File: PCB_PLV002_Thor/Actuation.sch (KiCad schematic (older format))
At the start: 58 parts, among them J20 Conn_01x02, J21 Conn_01x02, J22 Conn_01x02, J23 Conn_01x02, J24 Conn_01x02, J25 Conn_01x02, J26 Conn_01x02, J27 Conn_01x02, J28 Conn_01x02, J29 Conn_01x02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

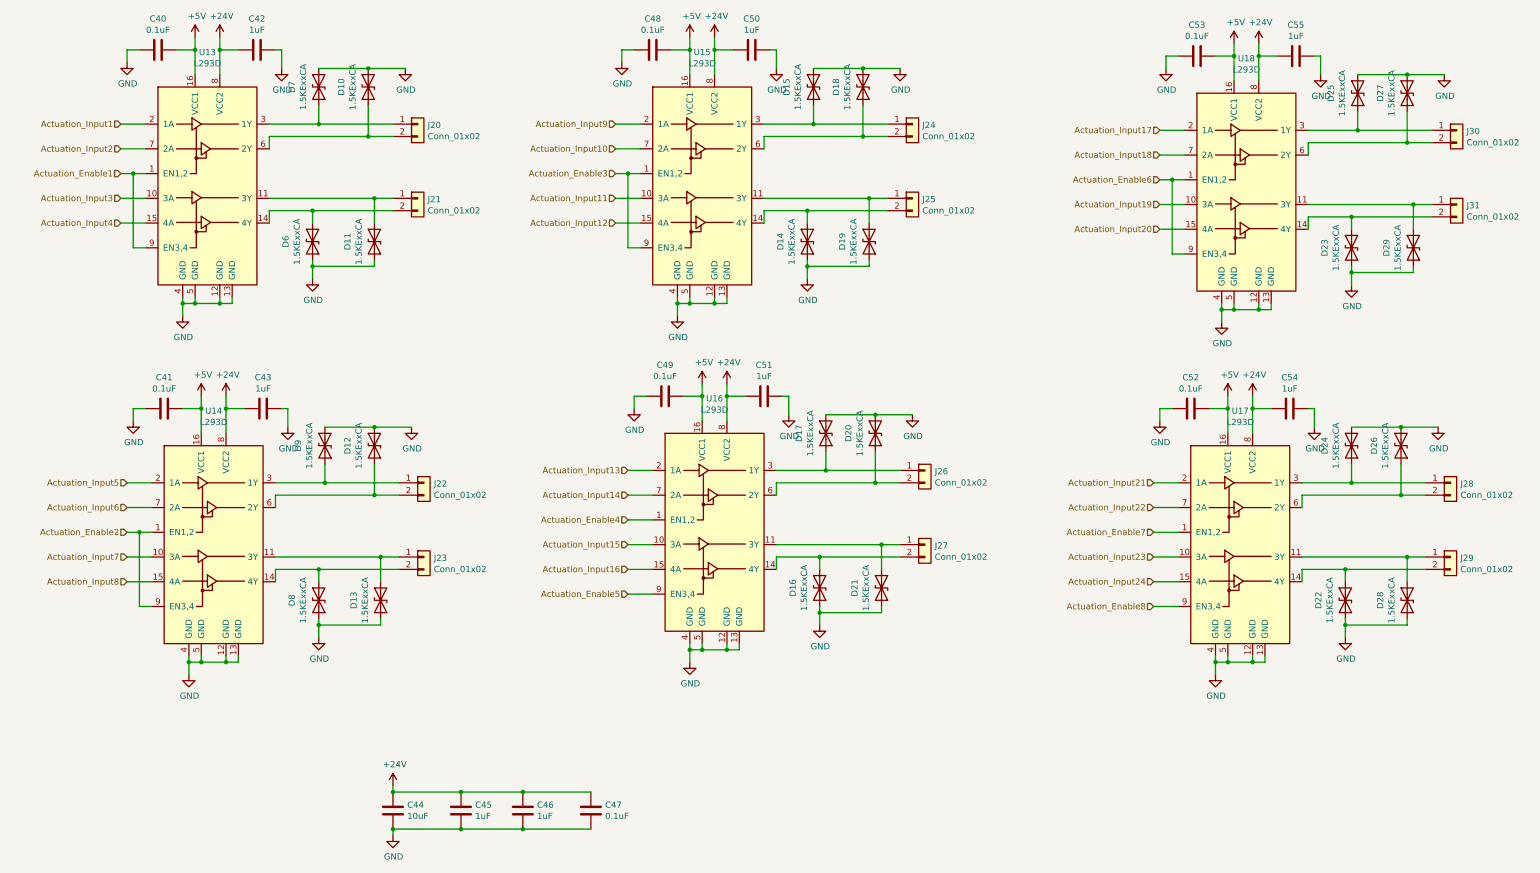
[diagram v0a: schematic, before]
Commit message: Schematic fix of actuator drivers
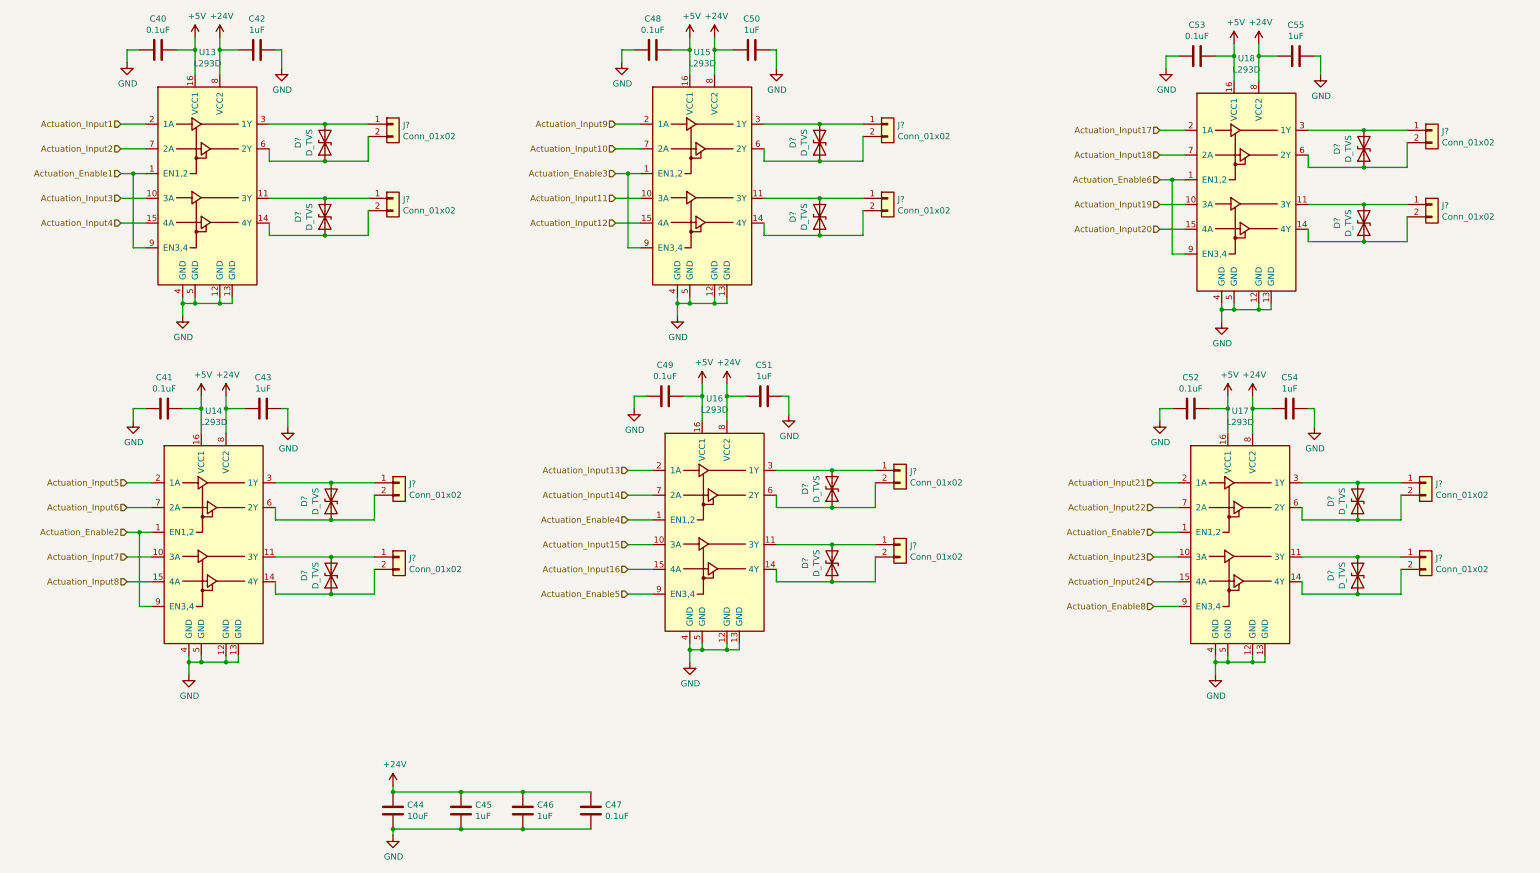
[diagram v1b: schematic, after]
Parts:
- removed D10, D11, D12, D13, D14, D15, D16, D17, D18, D19, D20, D21, D22, D23, D24, D25, D26, D27, D28, D29, D6, D7, D8, D9: 1.5KExxCA, Diode_THT:D_DO-201AE_P15.24mm_Horizontal, symbol Diode:1.5KExxCA
- removed J20, J21, J22, J23, J24, J25, J26, J27, J28, J29, J30, J31: Conn_01x02, Connector_Molex:Molex_Micro-Fit_3.0_43045-0200_2x01_P3.00mm_Horizontal, symbol Connector_Generic:Conn_01x02
- added D? (x12): D_TVS, symbol Device:D_TVS
- added J? (x12): Conn_01x02, Connector_Molex:Molex_Micro-Fit_3.0_43045-0200_2x01_P3.00mm_Horizontal, symbol Connector_Generic:Conn_01x02
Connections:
- net at U13.3 (1Y): now also D?.2 (A2), J?.1 (Pin_1)
- net at U13.6 (2Y): now also D?.1 (A1), J?.2 (Pin_2)
- net at U13.11 (3Y): now also D?.2 (A2), J?.1 (Pin_1)
- net at U13.14 (4Y): now also D?.1 (A1), J?.2 (Pin_2)
- net at U15.3 (1Y): now also D?.2 (A2), J?.1 (Pin_1)
- net at U15.6 (2Y): now also D?.1 (A1), J?.2 (Pin_2)
- net at U15.11 (3Y): now also D?.2 (A2), J?.1 (Pin_1)
- net at U15.14 (4Y): now also D?.1 (A1), J?.2 (Pin_2)
- net at U18.3 (1Y): now also D?.2 (A2), J?.1 (Pin_1)
- net at U18.6 (2Y): now also D?.1 (A1), J?.2 (Pin_2)
- net at U18.11 (3Y): now also D?.2 (A2), J?.1 (Pin_1)
- net at U18.14 (4Y): now also D?.1 (A1), J?.2 (Pin_2)
- net at U14.3 (1Y): now also D?.2 (A2), J?.1 (Pin_1)
- net at U14.6 (2Y): now also D?.1 (A1), J?.2 (Pin_2)
- net at U14.11 (3Y): now also D?.2 (A2), J?.1 (Pin_1)
- net at U14.14 (4Y): now also D?.1 (A1), J?.2 (Pin_2)
- net at U16.3 (1Y): now also D?.2 (A2), J?.1 (Pin_1)
- net at U16.6 (2Y): now also D?.1 (A1), J?.2 (Pin_2)
- net at U16.11 (3Y): now also D?.2 (A2), J?.1 (Pin_1)
- net at U16.14 (4Y): now also D?.1 (A1), J?.2 (Pin_2)
- net at U17.3 (1Y): now also D?.2 (A2), J?.1 (Pin_1)
- net at U17.6 (2Y): now also D?.1 (A1), J?.2 (Pin_2)
- net at U17.11 (3Y): now also D?.2 (A2), J?.1 (Pin_1)
- net at U17.14 (4Y): now also D?.1 (A1), J?.2 (Pin_2)
